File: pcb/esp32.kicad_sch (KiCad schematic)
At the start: 8 parts, among them Q1 BC817, U1 ESP32-WROOM-32

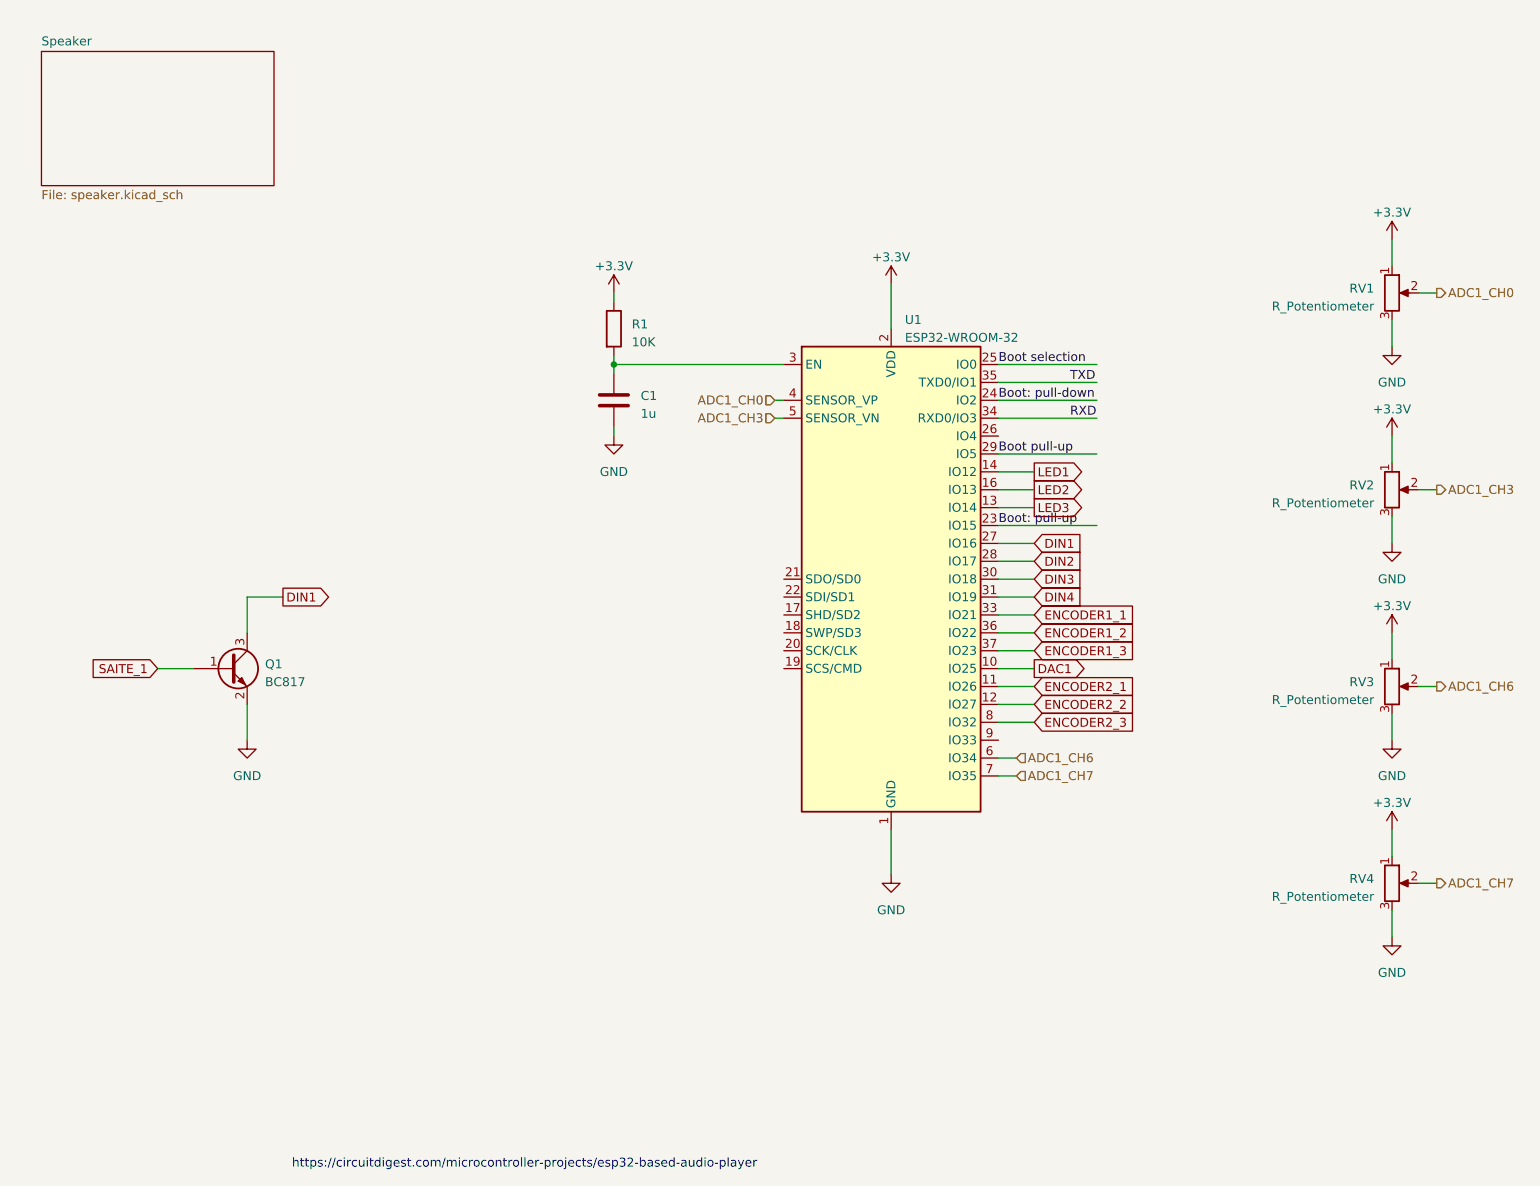
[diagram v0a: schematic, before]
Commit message: added some componentes to schematics and pcb
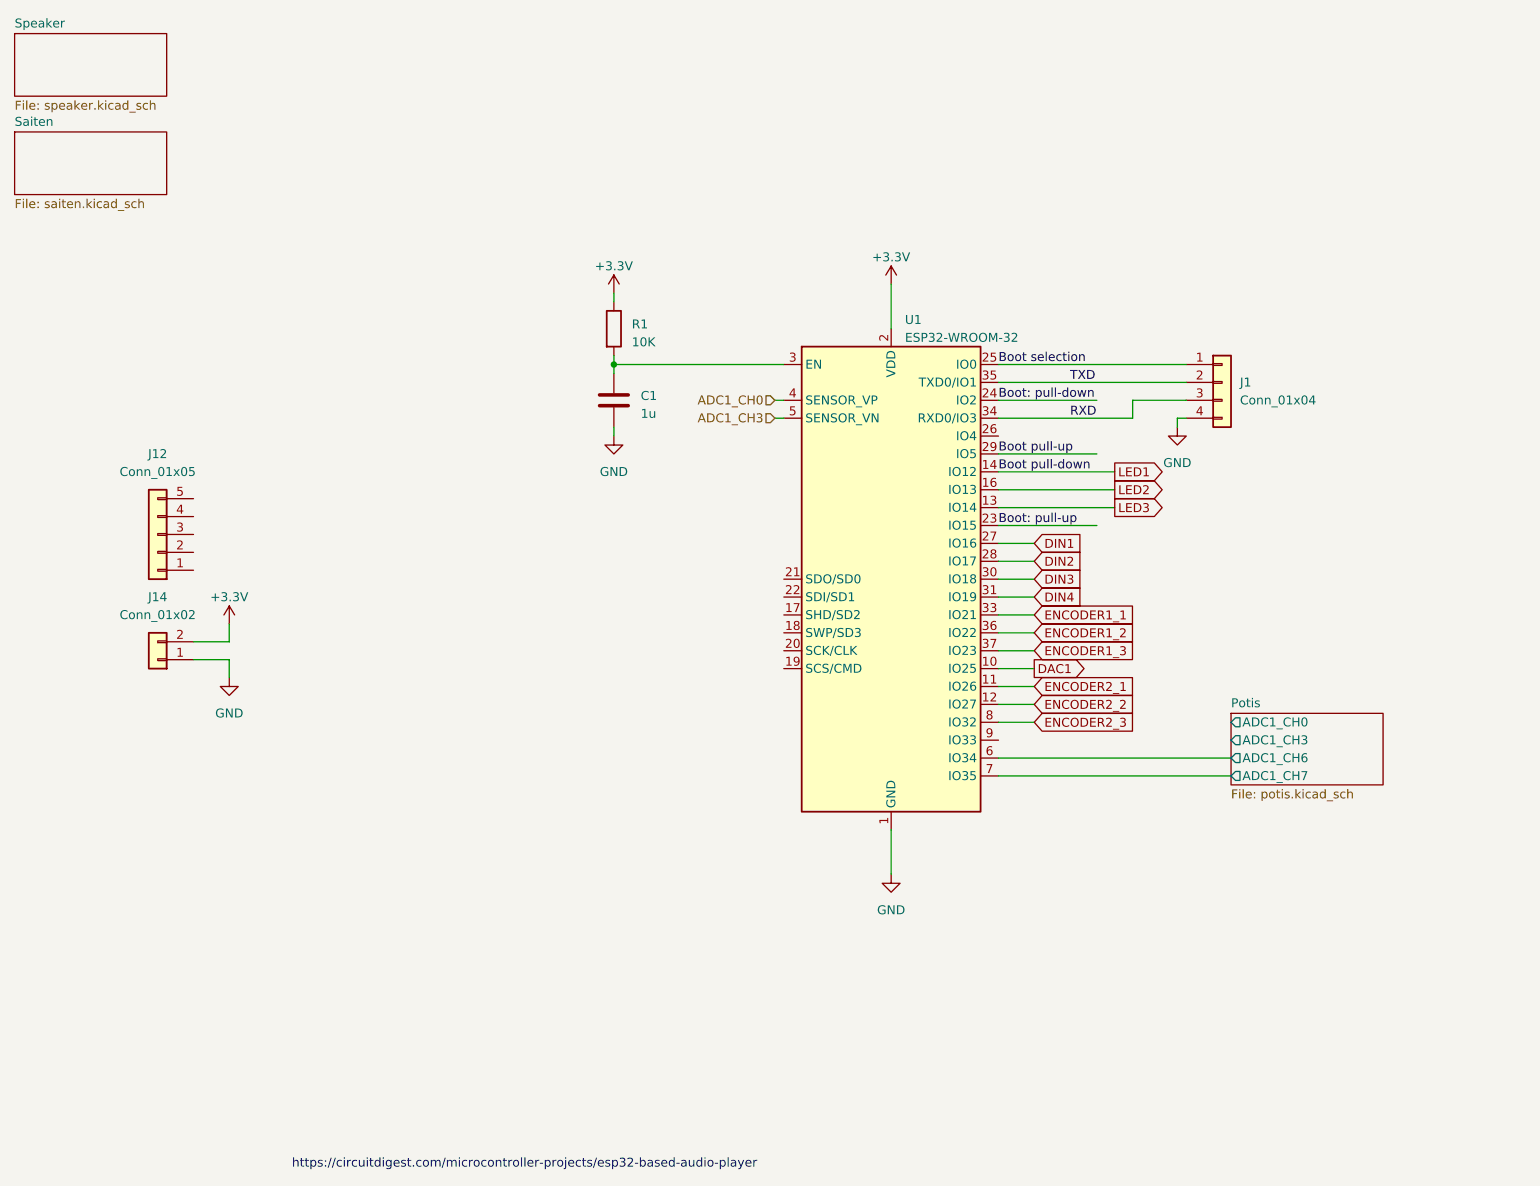
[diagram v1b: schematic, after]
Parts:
- removed Q1: BC817, Package_TO_SOT_SMD:SOT-23_Handsoldering, symbol Transistor_BJT:BC817
- removed RV1, RV2, RV3, RV4: R_Potentiometer, Potentiometer_THT:Potentiometer_ACP_CA6-H2,5_Horizontal, symbol Device:R_Potentiometer
- added J1: Conn_01x04, Connector_PinHeader_2.54mm:PinHeader_1x04_P2.54mm_Horizontal, symbol Connector_Generic:Conn_01x04
- added J12: Conn_01x05, Connector_PinHeader_2.54mm:PinHeader_1x05_P2.54mm_Vertical, symbol Connector_Generic:Conn_01x05
- added J14: Conn_01x02, Connector_PinHeader_2.54mm:PinHeader_1x02_P2.54mm_Vertical, symbol Connector_Generic:Conn_01x02
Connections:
- net +3.3V: now also J14.2 (Pin_2)
- net Boot selection: now also J1.1 (Pin_1)
- net GND: now also J1.4 (Pin_4), J14.1 (Pin_1)
- net RXD: now also J1.3 (Pin_3)
- net TXD: now also J1.2 (Pin_2)
- net ADC1_CH6 renamed Potis/ADC1_CH6
- net ADC1_CH7 renamed Potis/ADC1_CH7
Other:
- added sheet Potis (potis.kicad_sch)
- added sheet Saiten (saiten.kicad_sch)
- title: (none) -> vbass
